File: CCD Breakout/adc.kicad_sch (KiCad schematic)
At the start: 16 parts, among them U3 ADC-MCP33151

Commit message: Rev2 Fixes
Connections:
- net +5V: now also C14.1
- net GND: now also R15.1; no longer R16.1
- net opIND+: now also R16.2; no longer C14.1, R15.2
- new net: R15.2, R16.1, U4.4
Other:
- moved on the sheet: C14, R15, R16
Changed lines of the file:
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@@
 	(text_box "ADC"
 		(exclude_from_sim no)
-		(at 68.58 53.34 0)
-		(size 172.72 76.2)
+		(at 60.96 53.34 0)
+		(size 180.34 76.2)
 		(margins 0.9525 0.9525 0.9525 0.9525)
 		(stroke
@@
 	)
 	(junction
-		(at 116.84 107.95)
-		(diameter 0)
-		(color 0 0 0 0)
-	)
-	(junction
 		(at 190.5 73.66)
 		(diameter 0)
@@
 	)
 	(junction
-		(at 116.84 78.74)
-		(diameter 0)
-		(color 0 0 0 0)
-	)
-	(junction
 		(at 101.6 78.74)
 		(diameter 0)
@@
 	(wire
 		(pts
-			(xy 101.6 78.74) (xy 116.84 78.74)
+			(xy 101.6 78.74) (xy 128.27 78.74)
 		)
 		(stroke
@@
 	(wire
 		(pts
-			(xy 116.84 106.68) (xy 116.84 107.95)
+			(xy 72.39 100.33) (xy 72.39 102.87)
 		)
 		(stroke
@@
 	(wire
 		(pts
-			(xy 116.84 78.74) (xy 116.84 99.06)
-		)
-		(stroke
-			(width 0)
-			(type default)
-		)
-	)
-	(wire
-		(pts
 			(xy 82.55 76.2) (xy 82.55 78.74)
 		)
@@
 	(wire
 		(pts
-			(xy 116.84 107.95) (xy 128.27 107.95)
+			(xy 101.6 107.95) (xy 128.27 107.95)
 		)
 		(stroke
@@
 	(wire
 		(pts
-			(xy 116.84 78.74) (xy 128.27 78.74)
+			(xy 72.39 90.17) (xy 82.55 90.17)
 		)
 		(stroke
@@
 	(wire
 		(pts
-			(xy 101.6 107.95) (xy 116.84 107.95)
-		)
-		(stroke
-			(width 0)
-			(type default)
-		)
-	)
-	(wire
-		(pts
 			(xy 139.7 91.44) (xy 158.75 91.44)
+		)
+		(stroke
+			(width 0)
+			(type default)
+		)
+	)
+	(wire
+		(pts
+			(xy 72.39 92.71) (xy 72.39 90.17)
+		)
+		(stroke
+			(width 0)
+			(type default)
+		)
+	)
+	(wire
+		(pts
+			(xy 72.39 102.87) (xy 82.55 102.87)
 		)
 		(stroke
@@
 	(symbol
 		(lib_id "Device:R_US")
-		(at 128.27 86.36 180)
+		(at 128.27 102.87 180)
 		(unit 1)
 		(exclude_from_sim no)
@@
 		(fields_autoplaced yes)
 		(property "Reference" "R15"
-			(at 130.81 85.0899 0)
+			(at 130.81 101.5999 0)
 			(effects
 				(font
@@
 		)
 		(property "Value" "10k"
-			(at 130.81 87.6299 0)
+			(at 130.81 104.1399 0)
 			(effects
 				(font
@@
 		)
 		(property "Footprint" "Resistor_SMD:R_0603_1608Metric_Pad0.98x0.95mm_HandSolder"
-			(at 127.254 86.106 90)
+			(at 127.254 102.616 90)
 			(effects
 				(font
@@
 		)
 		(property "Datasheet" "~"
-			(at 128.27 86.36 0)
+			(at 128.27 102.87 0)
 			(effects
 				(font
@@
 		)
 		(property "Description" "Resistor, US symbol"
-			(at 128.27 86.36 0)
+			(at 128.27 102.87 0)
 			(effects
 				(font
@@
 	(symbol
 		(lib_id "Device:C_US")
-		(at 116.84 102.87 0)
+		(at 72.39 96.52 0)
 		(unit 1)
 		(exclude_from_sim no)
@@
 		(on_board yes)
 		(dnp no)
-		(fields_autoplaced yes)
 		(property "Reference" "C14"
-			(at 120.65 101.8539 0)
+			(at 65.024 95.758 0)
 			(effects
 				(font
@@
 		)
 		(property "Value" "0.47uF"
-			(at 120.65 104.3939 0)
+			(at 62.738 97.79 0)
 			(effects
 				(font
@@
 		)
 		(property "Footprint" "Capacitor_Tantalum_SMD:CP_EIA-2012-12_Kemet-R_HandSolder"
-			(at 116.84 102.87 0)
+			(at 72.39 96.52 0)
 			(effects
 				(font
@@
 		)
 		(property "Datasheet" ""
-			(at 116.84 102.87 0)
+			(at 72.39 96.52 0)
 			(effects
 				(font
@@
 		)
 		(property "Description" "capacitor, US symbol"
-			(at 116.84 102.87 0)
+			(at 72.39 96.52 0)
 			(effects
 				(font
@@
 	(symbol
 		(lib_id "Device:R_US")
-		(at 128.27 102.87 180)
+		(at 128.27 86.36 180)
 		(unit 1)
 		(exclude_from_sim no)
@@
 		(dnp no)
 		(property "Reference" "R16"
-			(at 130.81 101.5999 0)
+			(at 130.81 85.0899 0)
 			(effects
 				(font
@@
 		)
 		(property "Value" "20k"
-			(at 130.81 104.14 0)
+			(at 130.81 87.63 0)
 			(effects
 				(font
@@
 		)
 		(property "Footprint" "Resistor_SMD:R_0603_1608Metric_Pad0.98x0.95mm_HandSolder"
-			(at 127.254 102.616 90)
+			(at 127.254 86.106 90)
 			(effects
 				(font
@@
 		)
 		(property "Datasheet" "~"
-			(at 128.27 102.87 0)
+			(at 128.27 86.36 0)
 			(effects
 				(font
@@
 		)
 		(property "Description" "Resistor, US symbol"
-			(at 128.27 102.87 0)
-			(effects
-				(font
+			(at 128.27 86.36 0)
+			(effects
+				(font

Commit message: Miscellaneous schematic fixes
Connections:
- net +5V: no longer C14.1
- net opIND+: now also C14.1
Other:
- note added: "ADC"
- moved on the sheet: C14, R15, R16
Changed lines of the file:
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@@
 	(generator_version "9.0")
 	(paper "A4")
-	(bezier
-		(pts
-			(xy 142.24 86.36) (xy 142.24 86.36) (xy 162.56 81.28) (xy 162.56 81.28)
-		)
+	(rectangle
+		(start 60.96 41.91)
+		(end 254 142.24)
 		(stroke
 			(width 0)
@@
 	(bezier
 		(pts
-			(xy 162.56 81.28) (xy 162.56 81.28) (xy 142.24 76.2) (xy 142.24 76.2)
+			(xy 142.24 86.36) (xy 142.24 86.36) (xy 162.56 81.28) (xy 162.56 81.28)
 		)
 		(stroke
@@
 	(bezier
 		(pts
-			(xy 142.24 86.36) (xy 142.24 76.2) (xy 142.24 76.2) (xy 142.24 76.2)
+			(xy 162.56 81.28) (xy 162.56 81.28) (xy 142.24 76.2) (xy 142.24 76.2)
 		)
 		(stroke
@@
 		)
 	)
-	(text_box "ADC"
-		(exclude_from_sim no)
-		(at 60.96 53.34 0)
-		(size 180.34 76.2)
-		(margins 0.9525 0.9525 0.9525 0.9525)
-		(stroke
-			(width 0)
-			(type solid)
+	(bezier
+		(pts
+			(xy 142.24 86.36) (xy 142.24 76.2) (xy 142.24 76.2) (xy 142.24 76.2)
+		)
+		(stroke
+			(width 0)
+			(type default)
 		)
 		(fill
 			(type none)
 		)
+	)
+	(text "ADC"
+		(exclude_from_sim no)
+		(at 65.532 45.72 0)
 		(effects
 			(font
 				(size 1.27 1.27)
 			)
-			(justify left top)
 		)
 	)
@@
 	)
 	(junction
+		(at 118.11 107.95)
+		(diameter 0)
+		(color 0 0 0 0)
+	)
+	(junction
+		(at 118.11 78.74)
+		(diameter 0)
+		(color 0 0 0 0)
+	)
+	(junction
 		(at 82.55 102.87)
 		(diameter 0)
@@
 	)
 	(junction
-		(at 128.27 96.52)
+		(at 118.11 96.52)
 		(diameter 0)
 		(color 0 0 0 0)
@@
 	)
 	(junction
-		(at 215.9 87.63)
+		(at 133.35 78.74)
 		(diameter 0)
 		(color 0 0 0 0)
 	)
 	(junction
-		(at 128.27 78.74)
+		(at 215.9 87.63)
 		(diameter 0)
 		(color 0 0 0 0)
@@
 	(wire
 		(pts
-			(xy 128.27 78.74) (xy 128.27 82.55)
+			(xy 118.11 78.74) (xy 118.11 82.55)
 		)
 		(stroke
@@
 	(wire
 		(pts
+			(xy 133.35 78.74) (xy 142.24 78.74)
+		)
+		(stroke
+			(width 0)
+			(type default)
+		)
+	)
+	(wire
+		(pts
 			(xy 101.6 78.74) (xy 101.6 85.09)
 		)
@@
 	(wire
 		(pts
-			(xy 101.6 78.74) (xy 128.27 78.74)
-		)
-		(stroke
-			(width 0)
-			(type default)
-		)
-	)
-	(wire
-		(pts
-			(xy 111.76 96.52) (xy 128.27 96.52)
+			(xy 101.6 78.74) (xy 118.11 78.74)
+		)
+		(stroke
+			(width 0)
+			(type default)
+		)
+	)
+	(wire
+		(pts
+			(xy 111.76 96.52) (xy 118.11 96.52)
 		)
 		(stroke
@@
 	(wire
 		(pts
-			(xy 72.39 100.33) (xy 72.39 102.87)
-		)
-		(stroke
-			(width 0)
-			(type default)
-		)
-	)
-	(wire
-		(pts
 			(xy 177.8 101.6) (xy 194.31 101.6)
 		)
@@
 	(wire
 		(pts
+			(xy 133.35 91.44) (xy 133.35 78.74)
+		)
+		(stroke
+			(width 0)
+			(type default)
+		)
+	)
+	(wire
+		(pts
 			(xy 190.5 104.14) (xy 190.5 106.68)
 		)
@@
 	(wire
 		(pts
+			(xy 133.35 107.95) (xy 118.11 107.95)
+		)
+		(stroke
+			(width 0)
+			(type default)
+		)
+	)
+	(wire
+		(pts
 			(xy 190.5 68.58) (xy 199.39 68.58)
 		)
@@
 	(wire
 		(pts
-			(xy 128.27 106.68) (xy 128.27 107.95)
+			(xy 118.11 106.68) (xy 118.11 107.95)
 		)
 		(stroke
@@
 	(wire
 		(pts
-			(xy 101.6 107.95) (xy 128.27 107.95)
-		)
-		(stroke
-			(width 0)
-			(type default)
-		)
-	)
-	(wire
-		(pts
-			(xy 128.27 78.74) (xy 142.24 78.74)
+			(xy 101.6 107.95) (xy 118.11 107.95)
 		)
 		(stroke
@@
 	(wire
 		(pts
+			(xy 118.11 78.74) (xy 133.35 78.74)
+		)
+		(stroke
+			(width 0)
+			(type default)
+		)
+	)
+	(wire
+		(pts
 			(xy 196.85 82.55) (xy 196.85 86.36)
 		)
@@
 	(wire
 		(pts
-			(xy 72.39 90.17) (xy 82.55 90.17)
-		)
-		(stroke
-			(width 0)
-			(type default)
-		)
-	)
-	(wire
-		(pts
 			(xy 177.8 76.2) (xy 177.8 81.28)
 		)
@@
 	(wire
 		(pts
+			(xy 133.35 99.06) (xy 133.35 107.95)
+		)
+		(stroke
+			(width 0)
+			(type default)
+		)
+	)
+	(wire
+		(pts
 			(xy 157.48 81.28) (xy 158.75 81.28)
 		)
@@
 	(wire
 		(pts
-			(xy 128.27 90.17) (xy 128.27 96.52)
+			(xy 118.11 90.17) (xy 118.11 96.52)
 		)
 		(stroke
@@
 	(wire
 		(pts
-			(xy 128.27 96.52) (xy 128.27 99.06)
+			(xy 118.11 96.52) (xy 118.11 99.06)
 		)
 		(stroke
@@
 		(pts
 			(xy 139.7 91.44) (xy 158.75 91.44)
-		)
-		(stroke
-			(width 0)
-			(type default)
-		)
-	)
-	(wire
-		(pts
-			(xy 72.39 92.71) (xy 72.39 90.17)
-		)
-		(stroke
-			(width 0)
-			(type default)
-		)
-	)
-	(wire
-		(pts
-			(xy 72.39 102.87) (xy 82.55 102.87)
 		)
 		(stroke
@@
 	(symbol
 		(lib_id "Device:R_US")
-		(at 128.27 102.87 180)
+		(at 118.11 102.87 180)
 		(unit 1)
 		(exclude_from_sim no)
@@
 		(fields_autoplaced yes)
 		(property "Reference" "R15"
-			(at 130.81 101.5999 0)
+			(at 120.65 101.5999 0)
 			(effects
 				(font
@@
 		)
 		(property "Value" "10k"
-			(at 130.81 104.1399 0)
+			(at 120.65 104.1399 0)
 			(effects
 				(font
@@
 		)
 		(property "Footprint" "Resistor_SMD:R_0603_1608Metric_Pad0.98x0.95mm_HandSolder"
-			(at 127.254 102.616 90)
+			(at 117.094 102.616 90)
 			(effects
 				(font
@@
 		)
 		(property "Datasheet" "~"
-			(at 128.27 102.87 0)
+			(at 118.11 102.87 0)
 			(effects
 				(font
@@
 		)
 		(property "Description" "Resistor, US symbol"
-			(at 128.27 102.87 0)
+			(at 118.11 102.87 0)
 			(effects
 				(font
@@
 	(symbol
 		(lib_id "Device:C_US")
-		(at 72.39 96.52 0)
+		(at 133.35 95.25 0)
 		(unit 1)
 		(exclude_from_sim no)
@@
 		(dnp no)
 		(property "Reference" "C14"
-			(at 65.024 95.758 0)
+			(at 125.984 94.488 0)
 			(effects
 				(font
@@
 		)
 		(property "Value" "0.47uF"
-			(at 62.738 97.79 0)
+			(at 123.698 96.52 0)
 			(effects
 				(font
@@
 		)
 		(property "Footprint" "Capacitor_Tantalum_SMD:CP_EIA-2012-12_Kemet-R_HandSolder"
-			(at 72.39 96.52 0)
+			(at 133.35 95.25 0)
 			(effects
 				(font
@@
 		)
 		(property "Datasheet" ""
-			(at 72.39 96.52 0)
+			(at 133.35 95.25 0)
 			(effects
 				(font
@@
 		)
 		(property "Description" "capacitor, US symbol"
-			(at 72.39 96.52 0)
+			(at 133.35 95.25 0)
 			(effects
 				(font
@@
 		)
 		(instances
-			(project ""
+			(project "CCD_Breakout"
 				(path "/102965ac-29c6-4f96-94a4-d07431f6d693/a53142f3-0354-4e7c-bbfe-f09d56efc2e2"
 					(reference "TP1")
@@
 	(symbol
 		(lib_id "Device:R_US")
-		(at 128.27 86.36 180)
+		(at 118.11 86.36 180)
 		(unit 1)
 		(exclude_from_sim no)
@@
 		(dnp no)
 		(property "Reference" "R16"
-			(at 130.81 85.0899 0)
+			(at 120.65 85.0899 0)
 			(effects
 				(font
@@
 		)
 		(property "Value" "20k"
-			(at 130.81 87.63 0)
+			(at 120.65 87.63 0)
 			(effects
 				(font
@@
 		)
 		(property "Footprint" "Resistor_SMD:R_0603_1608Metric_Pad0.98x0.95mm_HandSolder"
-			(at 127.254 86.106 90)
+			(at 117.094 86.106 90)
 			(effects
 				(font
@@
 		)
 		(property "Datasheet" "~"
-			(at 128.27 86.36 0)
+			(at 118.11 86.36 0)
 			(effects
 				(font
@@
 		)
 		(property "Description" "Resistor, US symbol"
-			(at 128.27 86.36 0)
+			(at 118.11 86.36 0)
 			(effects
 				(font
@@
 		)
 		(instances
-			(project ""
+			(project "CCD_Breakout"
 				(path "/102965ac-29c6-4f96-94a4-d07431f6d693/a53142f3-0354-4e7c-bbfe-f09d56efc2e2"
 					(reference "#PWR03")
@@
 		)
 		(instances
-			(project ""
+			(project "CCD_Breakout"
 				(path "/102965ac-29c6-4f96-94a4-d07431f6d693/a53142f3-0354-4e7c-bbfe-f09d56efc2e2"
 					(reference "#PWR026")
@@
 		)
 		(instances
-			(project ""
+			(project "CCD_Breakout"
 				(path "/102965ac-29c6-4f96-94a4-d07431f6d693/a53142f3-0354-4e7c-bbfe-f09d56efc2e2"
 					(reference "C16")
@@
 		)
 		(instances
-			(project ""
+			(project "CCD_Breakout"
 				(path "/102965ac-29c6-4f96-94a4-d07431f6d693/a53142f3-0354-4e7c-bbfe-f09d56efc2e2"
 					(reference "#PWR010")
@@
 		)
 		(instances
-			(project ""
+			(project "CCD_Breakout"
 				(path "/102965ac-29c6-4f96-94a4-d07431f6d693/a53142f3-0354-4e7c-bbfe-f09d56efc2e2"
 					(reference "R7")
@@
 		)
 		(instances
-			(project ""
+			(project "CCD_Breakout"
 				(path "/102965ac-29c6-4f96-94a4-d07431f6d693/a53142f3-0354-4e7c-bbfe-f09d56efc2e2"
 					(reference "#PWR011")
@@
 		)
 		(instances
-			(project ""
+			(project "CCD_Breakout"
 				(path "/102965ac-29c6-4f96-94a4-d07431f6d693/a53142f3-0354-4e7c-bbfe-f09d56efc2e2"
 					(reference "C4")
@@
 		)
 		(instances
-			(project ""
+			(project "CCD_Breakout"
 				(path "/102965ac-29c6-4f96-94a4-d07431f6d693/a53142f3-0354-4e7c-bbfe-f09d56efc2e2"
 					(reference "U3")

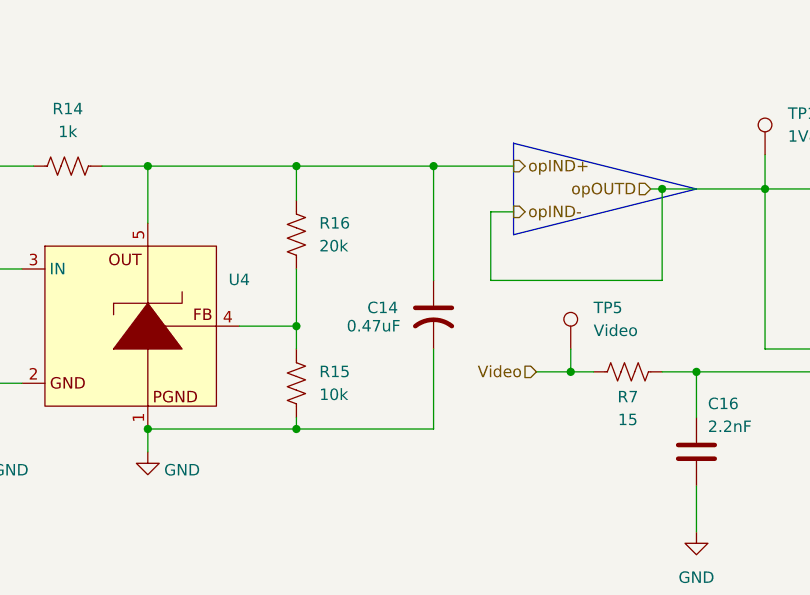
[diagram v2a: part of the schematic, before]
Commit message: Added 1uF capacitor to CMOS
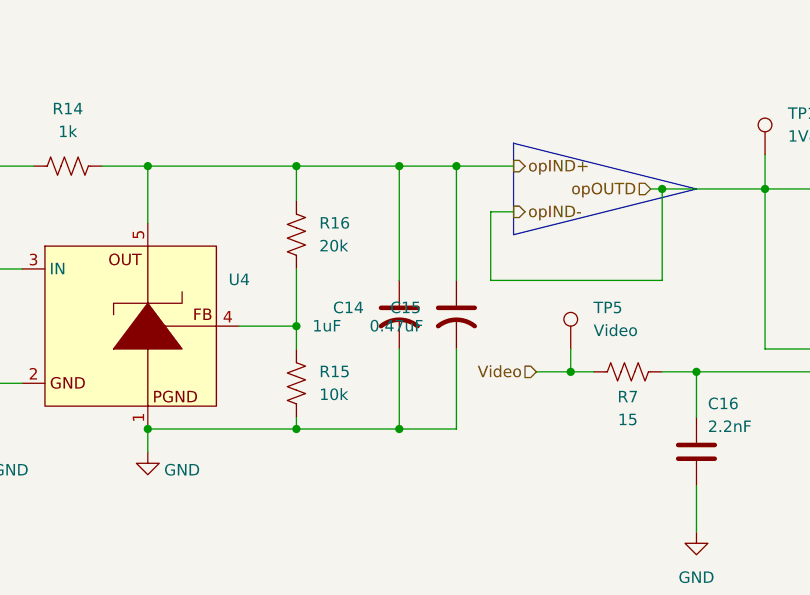
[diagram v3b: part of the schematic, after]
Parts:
- added C15: 0.47uF, Capacitor_Tantalum_SMD:CP_EIA-2012-12_Kemet-R_HandSolder, symbol Device:C_US
- C14: value 0.47uF -> 1uF
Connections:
- net GND: now also C15.2
- net opIND+: now also C15.1
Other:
- moved on the sheet: C14
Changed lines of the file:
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@@
+	)
+	(junction
+		(at 129.54 78.74)
+		(diameter 0)
+		(color 0 0 0 0)
 	)
 	(junction
@@
 	)
 	(junction
+		(at 135.89 78.74)
+		(diameter 0)
+		(color 0 0 0 0)
+	)
+	(junction
 		(at 190.5 68.58)
 		(diameter 0)
@@
 	)
 	(junction
-		(at 133.35 78.74)
-		(diameter 0)
-		(color 0 0 0 0)
-	)
-	(junction
 		(at 215.9 87.63)
 		(diameter 0)
@@
 		(color 0 0 0 0)
 	)
+	(junction
+		(at 129.54 107.95)
+		(diameter 0)
+		(color 0 0 0 0)
+	)
 	(wire
 		(pts
@@
 	(wire
 		(pts
+			(xy 135.89 107.95) (xy 129.54 107.95)
+		)
+		(stroke
+			(width 0)
+			(type default)
+		)
+	)
+	(wire
+		(pts
 			(xy 82.55 90.17) (xy 87.63 90.17)
 		)
@@
 	(wire
 		(pts
+			(xy 135.89 99.06) (xy 135.89 107.95)
+		)
+		(stroke
+			(width 0)
+			(type default)
+		)
+	)
+	(wire
+		(pts
 			(xy 148.59 101.6) (xy 151.13 101.6)
 		)
@@
 	(wire
 		(pts
-			(xy 133.35 78.74) (xy 142.24 78.74)
-		)
-		(stroke
-			(width 0)
-			(type default)
-		)
-	)
-	(wire
-		(pts
 			(xy 101.6 78.74) (xy 101.6 85.09)
 		)
@@
 	(wire
 		(pts
+			(xy 129.54 78.74) (xy 135.89 78.74)
+		)
+		(stroke
+			(width 0)
+			(type default)
+		)
+	)
+	(wire
+		(pts
 			(xy 162.56 101.6) (xy 162.56 106.68)
 		)
@@
 	(wire
 		(pts
-			(xy 133.35 91.44) (xy 133.35 78.74)
+			(xy 129.54 91.44) (xy 129.54 78.74)
+		)
+		(stroke
+			(width 0)
+			(type default)
+		)
+	)
+	(wire
+		(pts
+			(xy 135.89 78.74) (xy 135.89 91.44)
 		)
 		(stroke
@@
 	(wire
 		(pts
-			(xy 133.35 107.95) (xy 118.11 107.95)
+			(xy 129.54 107.95) (xy 118.11 107.95)
 		)
 		(stroke
@@
 	(wire
 		(pts
+			(xy 135.89 78.74) (xy 142.24 78.74)
+		)
+		(stroke
+			(width 0)
+			(type default)
+		)
+	)
+	(wire
+		(pts
 			(xy 82.55 102.87) (xy 87.63 102.87)
 		)
@@
 	(wire
 		(pts
-			(xy 118.11 78.74) (xy 133.35 78.74)
+			(xy 118.11 78.74) (xy 129.54 78.74)
 		)
 		(stroke
@@
 	(wire
 		(pts
-			(xy 133.35 99.06) (xy 133.35 107.95)
+			(xy 129.54 99.06) (xy 129.54 107.95)
 		)
 		(stroke
@@
 	(symbol
 		(lib_id "Device:C_US")
-		(at 133.35 95.25 0)
+		(at 129.54 95.25 0)
 		(unit 1)
 		(exclude_from_sim no)
@@
 		(dnp no)
 		(property "Reference" "C14"
-			(at 125.984 94.488 0)
+			(at 122.174 94.488 0)
 			(effects
 				(font
@@
 			)
 		)
-		(property "Value" "0.47uF"
-			(at 123.698 96.52 0)
+		(property "Value" "1uF"
+			(at 119.888 96.52 0)
 			(effects
 				(font
@@
 		)
 		(property "Footprint" "Capacitor_Tantalum_SMD:CP_EIA-2012-12_Kemet-R_HandSolder"
-			(at 133.35 95.25 0)
+			(at 129.54 95.25 0)
 			(effects
 				(font
@@
 		)
 		(property "Datasheet" ""
-			(at 133.35 95.25 0)
+			(at 129.54 95.25 0)
 			(effects
 				(font
@@
 		)
 		(property "Description" "capacitor, US symbol"
-			(at 133.35 95.25 0)
+			(at 129.54 95.25 0)
 			(effects
 				(font
@@
 					(unit 1)
 				)
+			)
+		)
+	)
+	(symbol
+		(lib_id "Device:C_US")
+		(at 135.89 95.25 0)
+		(unit 1)
+		(exclude_from_sim no)
+		(in_bom yes)
+		(on_board yes)
+		(dnp no)
+		(property "Reference" "C15"
+			(at 128.524 94.488 0)
+			(effects
+				(font
+					(size 1.27 1.27)
+				)
+				(justify left)
+			)
+		)
+		(property "Value" "0.47uF"
+			(at 126.238 96.52 0)
+			(effects
+				(font
+					(size 1.27 1.27)
+				)
+				(justify left)
+			)
+		)
+		(property "Footprint" "Capacitor_Tantalum_SMD:CP_EIA-2012-12_Kemet-R_HandSolder"
+			(at 135.89 95.25 0)
+			(effects
+				(font
+					(size 1.27 1.27)
+				)
+				(hide yes)
+			)
+		)
+		(property "Datasheet" ""
+			(at 135.89 95.25 0)
+			(effects
+				(font
+					(size 1.27 1.27)
+				)
+				(hide yes)
+			)
+		)
+		(property "Description" "capacitor, US symbol"
+			(at 135.89 95.25 0)
+			(effects
+				(font
+					(size 1.27 1.27)
+				)
+				(hide yes)
+			)
+		)
+		(pin "2"
+		)
+		(pin "1"
+		)
+		(instances
+			(project "CCD_Breakout"
+				(path "/102965ac-29c6-4f96-94a4-d07431f6d693/a53142f3-0354-4e7c-bbfe-f09d56efc2e2"
+					(reference "C15")
+					(unit 1)
+				)
